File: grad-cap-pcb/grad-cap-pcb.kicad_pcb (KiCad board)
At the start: 2 copper layers, 323.3 x 323.3 mm, 146 parts

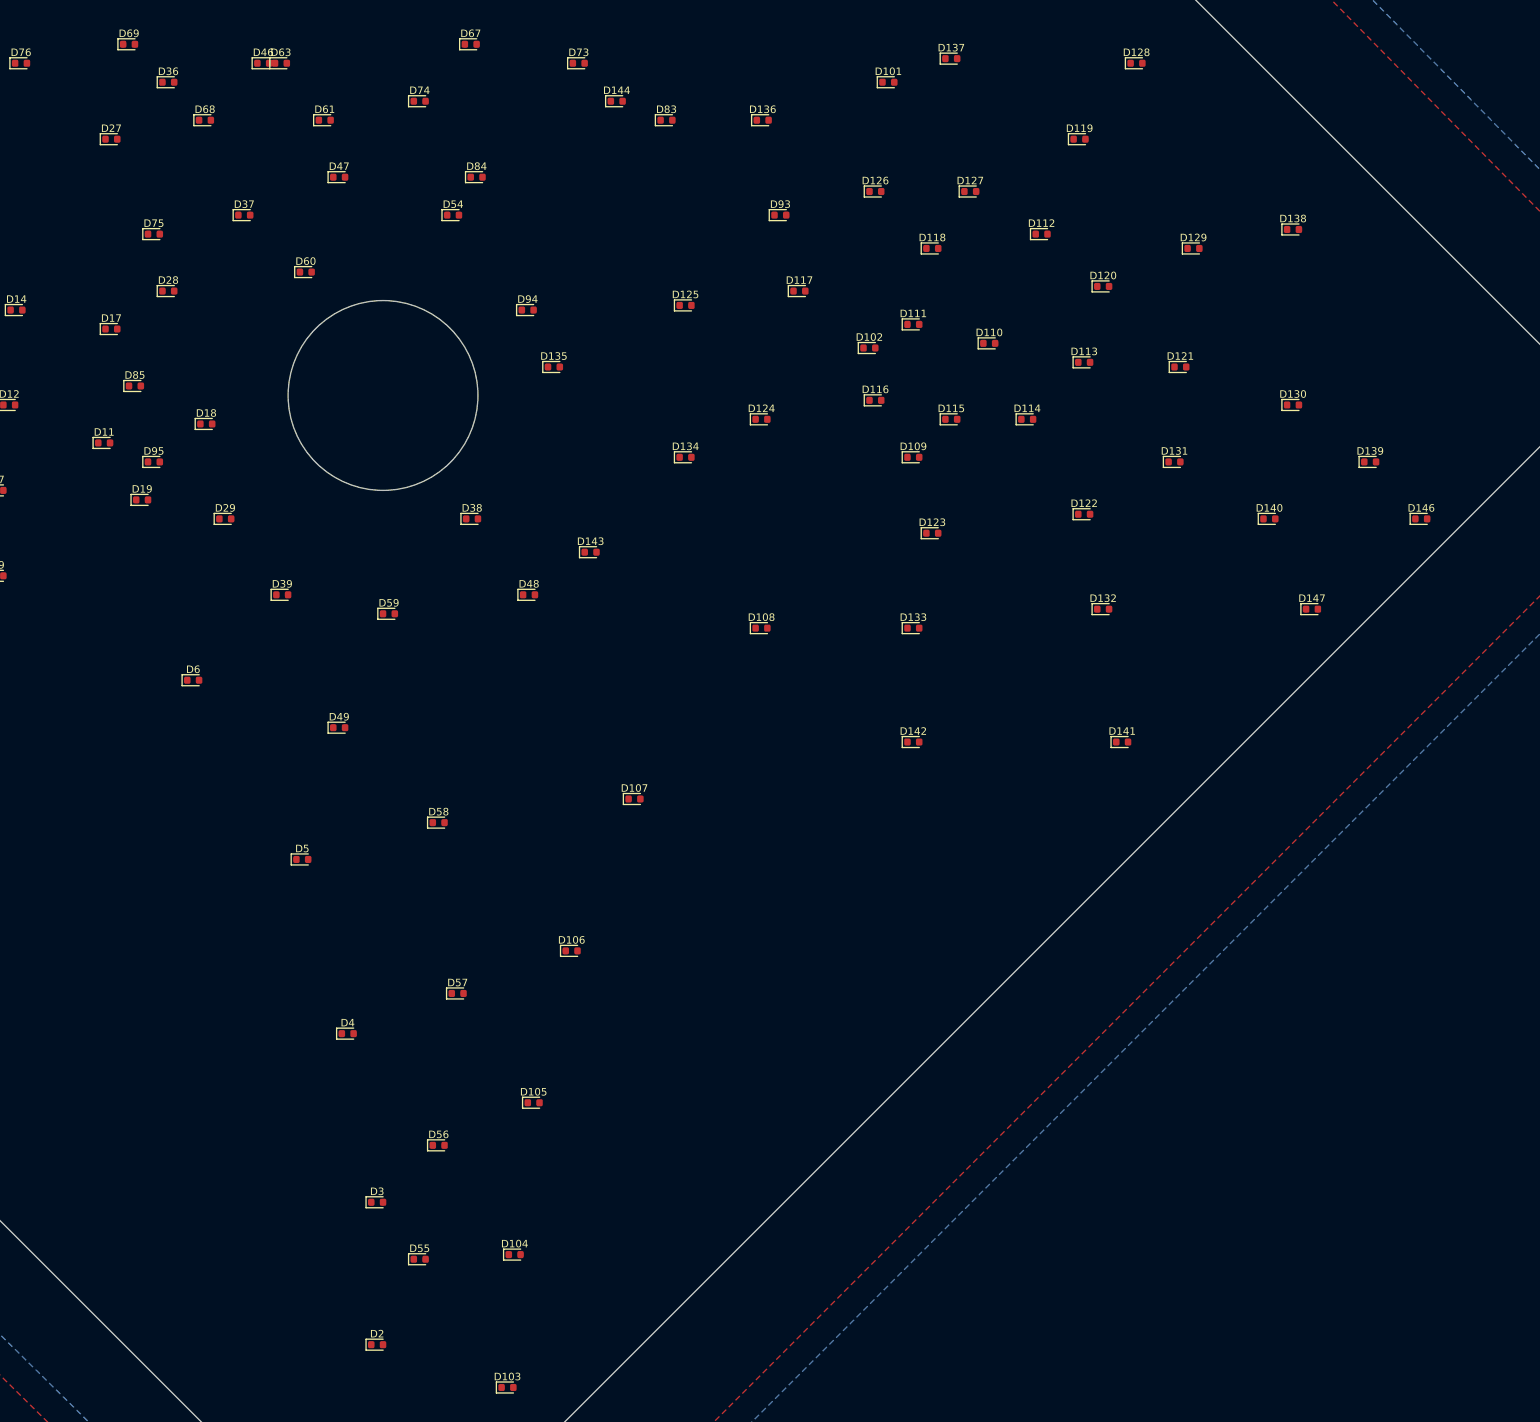
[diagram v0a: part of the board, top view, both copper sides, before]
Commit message: addd more
switched from npn to pnp to make the LEDs connect to the ground plane - easier routing.
added labels and or gates so the mosfets wouldnt trigger each other
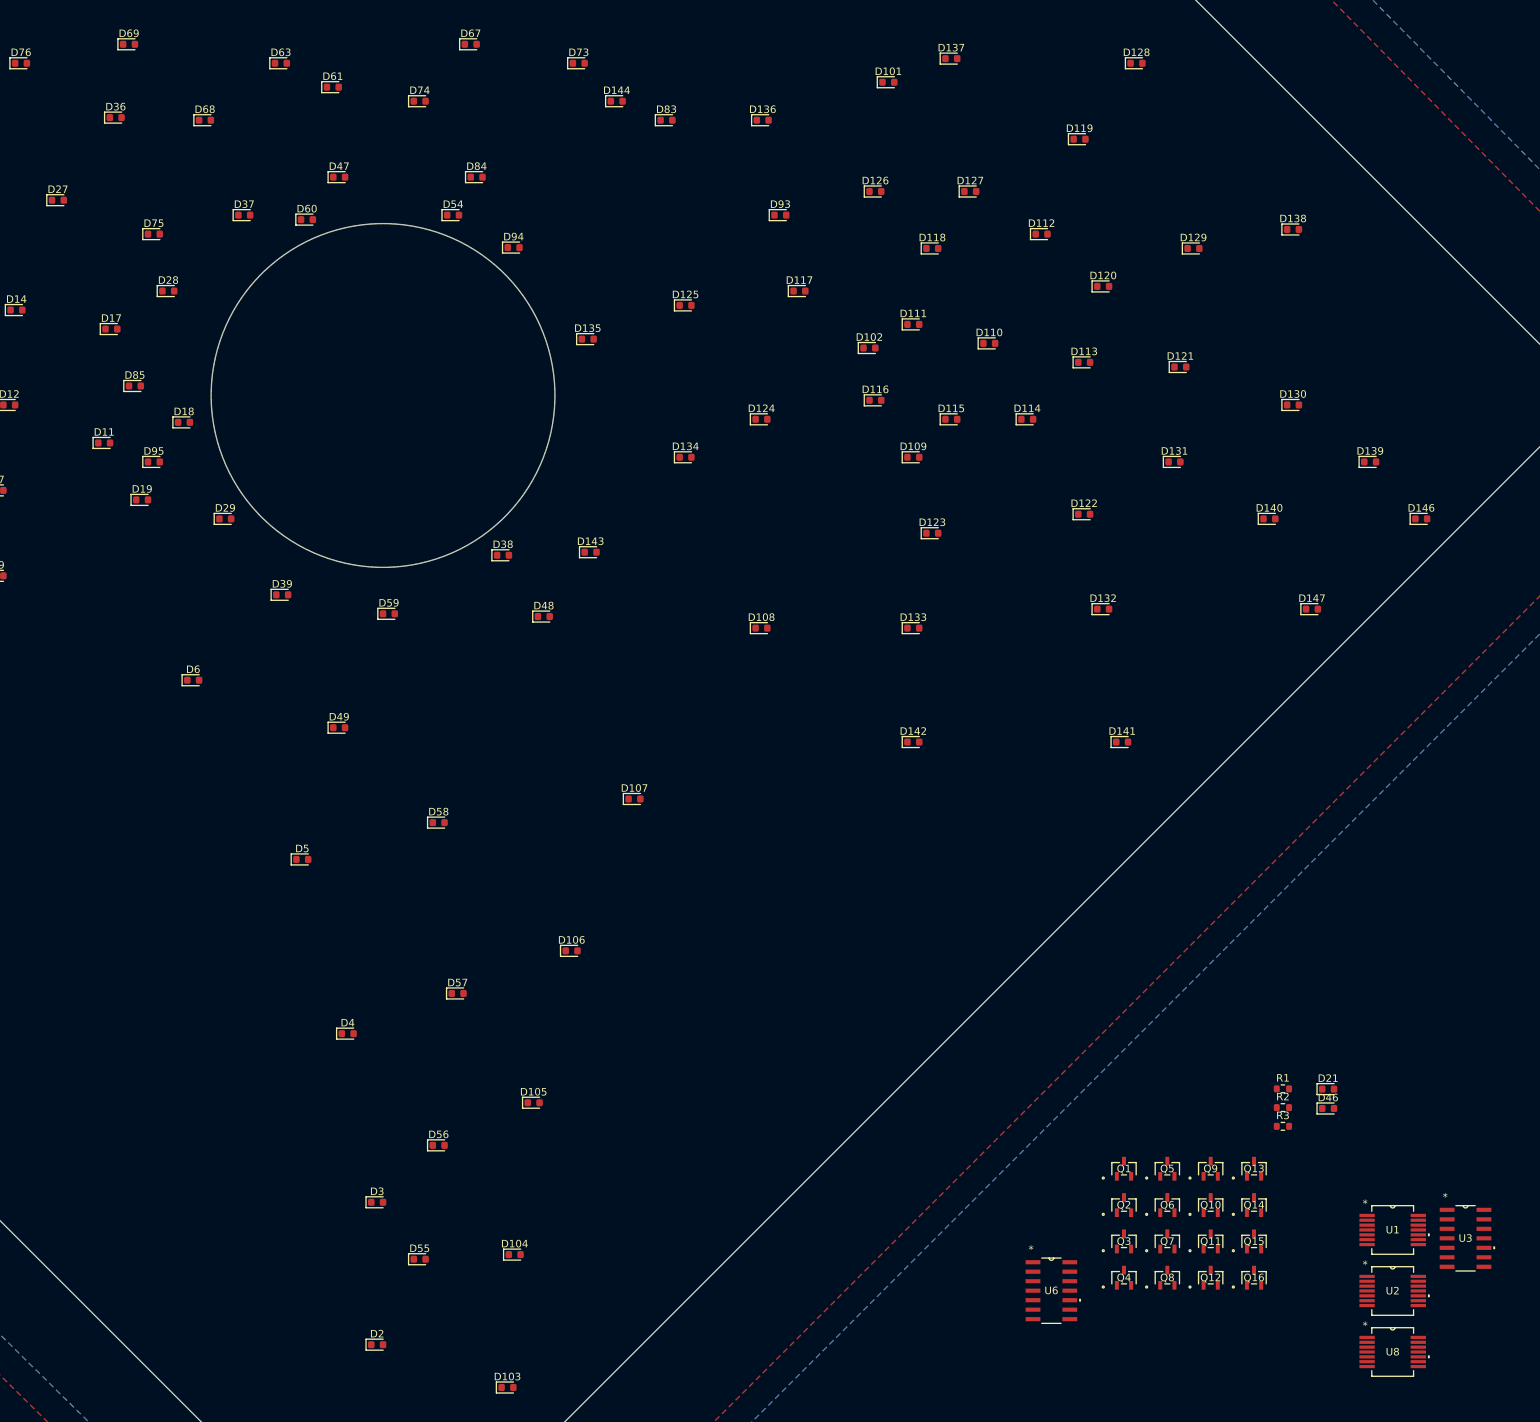
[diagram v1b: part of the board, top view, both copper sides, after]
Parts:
- added D21: LED, LED_SMD:LED_0603_1608Metric, F.Cu at (380.5, 315.1)
- added Q1: NPN, General Library:PN2907A, F.Cu at (353.1, 325.7)
- added Q10: NPN, General Library:PN2907A, F.Cu at (364.7, 330.6)
- added Q11: NPN, General Library:PN2907A, F.Cu at (364.7, 335.4)
- added Q12: NPN, General Library:PN2907A, F.Cu at (364.7, 340.3)
- added Q13: NPN, General Library:PN2907A, F.Cu at (370.5, 325.7)
- added Q14: NPN, General Library:PN2907A, F.Cu at (370.5, 330.6)
- added Q15: NPN, General Library:PN2907A, F.Cu at (370.5, 335.4)
- added Q16: NPN, General Library:PN2907A, F.Cu at (370.5, 340.3)
- added Q2: NPN, General Library:PN2907A, F.Cu at (353.1, 330.6)
- added Q3: NPN, General Library:PN2907A, F.Cu at (353.1, 335.4)
- added Q4: NPN, General Library:PN2907A, F.Cu at (353.1, 340.3)
- added Q5: NPN, General Library:PN2907A, F.Cu at (358.9, 325.7)
- added Q6: NPN, General Library:PN2907A, F.Cu at (358.9, 330.6)
- added Q7: NPN, General Library:PN2907A, F.Cu at (358.9, 335.4)
- added Q8: NPN, General Library:PN2907A, F.Cu at (358.9, 340.3)
- added Q9: NPN, General Library:PN2907A, F.Cu at (364.7, 325.7)
- added R1: 0 ohms, Resistor_SMD:R_0603_1608Metric, F.Cu at (374.4, 315.0)
- added R2: 0 ohms, Resistor_SMD:R_0603_1608Metric, F.Cu at (374.4, 317.5)
- added R3: 0 ohms, Resistor_SMD:R_0603_1608Metric, F.Cu at (374.4, 320.0)
- added U1: SN74AHCT32DBR, GRAD-CAP:SN74AHCT32DBR_2-INPUT-QUAD-OR, F.Cu at (389.1, 333.9)
- added U2: SN74AHCT32DBR, GRAD-CAP:SN74AHCT32DBR_2-INPUT-QUAD-OR, F.Cu at (389.1, 342.1)
- added U3: CD4072BM96, GRAD-CAP:CD4072BM96_4-INPUT-OR, F.Cu at (398.8, 335.0)
- added U6: CD4075BM96, GRAD-CAP:CD4075BM96-3IN-TRIO-OR, F.Cu at (343.4, 342.0)
- added U8: SN74AHCT32DBR, GRAD-CAP:SN74AHCT32DBR_2-INPUT-QUAD-OR, F.Cu at (389.1, 350.2)
- moved D46 199.6 mm to (380.5, 317.6)
- moved D27 10.9 mm to (210.5, 196.1)
- moved D94 8.57 mm to (271.5, 202.5)
- moved D36 8.49 mm to (218.2, 185.1)
- moved D60 7.02 mm to (243.8, 198.7)
- moved D38 6.39 mm to (270.1, 243.6)
- moved D135 5.87 mm to (281.4, 214.7)
- moved D61 4.55 mm to (247.3, 181.0)
- moved D48 3.52 mm to (275.5, 251.8)
- moved D18 2.99 mm to (227.4, 225.8)
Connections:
- D1 pad 1: unconnected-(D1-K-Pad1) -> /leds+mosfets/frame1
- D1 pad 2: unconnected-(D1-A-Pad2) -> +2V2
- D10 pad 1: unconnected-(D10-K-Pad1) -> /leds+mosfets/frame4
- D10 pad 2: unconnected-(D10-A-Pad2) -> +2V2
- D100 pad 1: unconnected-(D100-K-Pad1) -> /leds+mosfets/frame14
- D100 pad 2: unconnected-(D100-A-Pad2) -> +2V2
- D101 pad 1: unconnected-(D101-K-Pad1) -> /leds+mosfets/frame15
- D101 pad 2: unconnected-(D101-A-Pad2) -> +2V2
- D102 pad 1: unconnected-(D102-K-Pad1) -> /leds+mosfets/13or14
- D102 pad 2: unconnected-(D102-A-Pad2) -> +2V2
- D103 pad 1: unconnected-(D103-K-Pad1) -> /leds+mosfets/frame14
- D103 pad 2: unconnected-(D103-A-Pad2) -> +2V2
- D104 pad 1: unconnected-(D104-K-Pad1) -> /leds+mosfets/14or15
- D104 pad 2: unconnected-(D104-A-Pad2) -> +2V2
- D105 pad 1: unconnected-(D105-K-Pad1) -> /leds+mosfets/frame15
- D105 pad 2: unconnected-(D105-A-Pad2) -> +2V2
- D106 pad 1: unconnected-(D106-K-Pad1) -> /leds+mosfets/15or16
- D106 pad 2: unconnected-(D106-A-Pad2) -> +2V2
- D107 pad 1: unconnected-(D107-K-Pad1) -> /leds+mosfets/frame16
- D107 pad 2: unconnected-(D107-A-Pad2) -> +2V2
- D108 pad 1: unconnected-(D108-K-Pad1) -> /leds+mosfets/frame1
- D108 pad 2: unconnected-(D108-A-Pad2) -> +2V2
- D109 pad 1: unconnected-(D109-K-Pad1) -> /leds+mosfets/frame1
- D109 pad 2: unconnected-(D109-A-Pad2) -> +2V2
- D11 pad 1: unconnected-(D11-K-Pad1) -> /leds+mosfets/frame4
- D11 pad 2: unconnected-(D11-A-Pad2) -> +2V2
- D110 pad 1: unconnected-(D110-K-Pad1) -> /leds+mosfets/frame2
- D110 pad 2: unconnected-(D110-A-Pad2) -> +2V2
- D111 pad 1: unconnected-(D111-K-Pad1) -> /leds+mosfets/frame3
- D111 pad 2: unconnected-(D111-A-Pad2) -> +2V2
- D112 pad 1: unconnected-(D112-K-Pad1) -> /leds+mosfets/frame3
- D112 pad 2: unconnected-(D112-A-Pad2) -> +2V2
- D113 pad 1: unconnected-(D113-K-Pad1) -> /leds+mosfets/3or4
- D113 pad 2: unconnected-(D113-A-Pad2) -> +2V2
- D114 pad 1: unconnected-(D114-K-Pad1) -> /leds+mosfets/frame4
- D114 pad 2: unconnected-(D114-A-Pad2) -> +2V2
- D115 pad 1: unconnected-(D115-K-Pad1) -> /leds+mosfets/frame3
- D115 pad 2: unconnected-(D115-A-Pad2) -> +2V2
- D116 pad 1: unconnected-(D116-K-Pad1) -> /leds+mosfets/frame4
- D116 pad 2: unconnected-(D116-A-Pad2) -> +2V2
- D117 pad 1: unconnected-(D117-K-Pad1) -> /leds+mosfets/frame4
- D117 pad 2: unconnected-(D117-A-Pad2) -> +2V2
- D118 pad 1: unconnected-(D118-K-Pad1) -> /leds+mosfets/frame4
- D118 pad 2: unconnected-(D118-A-Pad2) -> +2V2
- D119 pad 1: unconnected-(D119-K-Pad1) -> /leds+mosfets/frame3
- D119 pad 2: unconnected-(D119-A-Pad2) -> +2V2
- D12 pad 1: unconnected-(D12-K-Pad1) -> /leds+mosfets/frame4
- D12 pad 2: unconnected-(D12-A-Pad2) -> +2V2
- D120 pad 1: unconnected-(D120-K-Pad1) -> /leds+mosfets/frame4
- D120 pad 2: unconnected-(D120-A-Pad2) -> +2V2
- D121 pad 1: unconnected-(D121-K-Pad1) -> /leds+mosfets/4or5
- D121 pad 2: unconnected-(D121-A-Pad2) -> +2V2
- D122 pad 1: unconnected-(D122-K-Pad1) -> /leds+mosfets/4or5
- D122 pad 2: unconnected-(D122-A-Pad2) -> +2V2
- D123 pad 1: unconnected-(D123-K-Pad1) -> /leds+mosfets/frame4
- D123 pad 2: unconnected-(D123-A-Pad2) -> +2V2
- D124 pad 1: unconnected-(D124-K-Pad1) -> /leds+mosfets/4or5
- D124 pad 2: unconnected-(D124-A-Pad2) -> +2V2
- D125 pad 1: unconnected-(D125-K-Pad1) -> /leds+mosfets/4or5
- D125 pad 2: unconnected-(D125-A-Pad2) -> +2V2
- D126 pad 1: unconnected-(D126-K-Pad1) -> /leds+mosfets/4or5
- D126 pad 2: unconnected-(D126-A-Pad2) -> +2V2
- D127 pad 1: unconnected-(D127-K-Pad1) -> /leds+mosfets/frame5
- D127 pad 2: unconnected-(D127-A-Pad2) -> +2V2
- D128 pad 1: unconnected-(D128-K-Pad1) -> /leds+mosfets/4or5
- D128 pad 2: unconnected-(D128-A-Pad2) -> +2V2
- D129 pad 1: unconnected-(D129-K-Pad1) -> /leds+mosfets/frame4
- D129 pad 2: unconnected-(D129-A-Pad2) -> +2V2
- D13 pad 1: unconnected-(D13-K-Pad1) -> /leds+mosfets/4or5
- D13 pad 2: unconnected-(D13-A-Pad2) -> +2V2
- D130 pad 1: unconnected-(D130-K-Pad1) -> /leds+mosfets/5or6
- D130 pad 2: unconnected-(D130-A-Pad2) -> +2V2
- D131 pad 1: unconnected-(D131-K-Pad1) -> /leds+mosfets/5or6
- D131 pad 2: unconnected-(D131-A-Pad2) -> +2V2
- D132 pad 1: unconnected-(D132-K-Pad1) -> /leds+mosfets/5or6
- D132 pad 2: unconnected-(D132-A-Pad2) -> +2V2
- D133 pad 1: unconnected-(D133-K-Pad1) -> /leds+mosfets/4or5
- D133 pad 2: unconnected-(D133-A-Pad2) -> +2V2
- D134 pad 1: unconnected-(D134-K-Pad1) -> /leds+mosfets/frame6
- D134 pad 2: unconnected-(D134-A-Pad2) -> +2V2
- D135 pad 1: unconnected-(D135-K-Pad1) -> /leds+mosfets/5or6
- D135 pad 2: unconnected-(D135-A-Pad2) -> +2V2
- D136 pad 1: unconnected-(D136-K-Pad1) -> /leds+mosfets/5or6
- D136 pad 2: unconnected-(D136-A-Pad2) -> +2V2
- D137 pad 1: unconnected-(D137-K-Pad1) -> /leds+mosfets/5or6
- D137 pad 2: unconnected-(D137-A-Pad2) -> +2V2
- D138 pad 1: unconnected-(D138-K-Pad1) -> /leds+mosfets/5or6
- D138 pad 2: unconnected-(D138-A-Pad2) -> +2V2
- D139 pad 1: unconnected-(D139-K-Pad1) -> /leds+mosfets/6or7
- D139 pad 2: unconnected-(D139-A-Pad2) -> +2V2
- D14 pad 1: unconnected-(D14-K-Pad1) -> /leds+mosfets/frame5
- D14 pad 2: unconnected-(D14-A-Pad2) -> +2V2
- D140 pad 1: unconnected-(D140-K-Pad1) -> /leds+mosfets/6or7
- D140 pad 2: unconnected-(D140-A-Pad2) -> +2V2
- D141 pad 1: unconnected-(D141-K-Pad1) -> /leds+mosfets/6or7
- D141 pad 2: unconnected-(D141-A-Pad2) -> +2V2
- D142 pad 1: unconnected-(D142-K-Pad1) -> /leds+mosfets/5or6or7or8
- D142 pad 2: unconnected-(D142-A-Pad2) -> +2V2
- D143 pad 1: unconnected-(D143-K-Pad1) -> /leds+mosfets/6or7or8
- D143 pad 2: unconnected-(D143-A-Pad2) -> +2V2
- D144 pad 1: unconnected-(D144-K-Pad1) -> /leds+mosfets/6or7or8
- D144 pad 2: unconnected-(D144-A-Pad2) -> +2V2
- D145 pad 1: unconnected-(D145-K-Pad1) -> /leds+mosfets/6or7
- D145 pad 2: unconnected-(D145-A-Pad2) -> +2V2
- D146 pad 1: unconnected-(D146-K-Pad1) -> /leds+mosfets/7or8
- D146 pad 2: unconnected-(D146-A-Pad2) -> +2V2
- D147 pad 1: unconnected-(D147-K-Pad1) -> /leds+mosfets/frame7
- D147 pad 2: unconnected-(D147-A-Pad2) -> +2V2
- D15 pad 1: unconnected-(D15-K-Pad1) -> /leds+mosfets/4or5
- D15 pad 2: unconnected-(D15-A-Pad2) -> +2V2
- D16 pad 1: unconnected-(D16-K-Pad1) -> /leds+mosfets/4or5
- D16 pad 2: unconnected-(D16-A-Pad2) -> +2V2
- D17 pad 1: unconnected-(D17-K-Pad1) -> /leds+mosfets/frame5
- D17 pad 2: unconnected-(D17-A-Pad2) -> +2V2
- D18 pad 1: unconnected-(D18-K-Pad1) -> /leds+mosfets/frame4
- D18 pad 2: unconnected-(D18-A-Pad2) -> +2V2
- D19 pad 2: unconnected-(D19-A-Pad2) -> GND
- D2 pad 1: unconnected-(D2-K-Pad1) -> /leds+mosfets/frame1
- D2 pad 2: unconnected-(D2-A-Pad2) -> +2V2
- D20 pad 1: unconnected-(D20-K-Pad1) -> /leds+mosfets/6or7
- D20 pad 2: unconnected-(D20-A-Pad2) -> +2V2
- D22 pad 1: unconnected-(D22-K-Pad1) -> /leds+mosfets/6or7
- D22 pad 2: unconnected-(D22-A-Pad2) -> +2V2
- D23 pad 1: unconnected-(D23-K-Pad1) -> /leds+mosfets/frame6
- D23 pad 2: unconnected-(D23-A-Pad2) -> +2V2
- D24 pad 1: unconnected-(D24-K-Pad1) -> /leds+mosfets/frame6
- D24 pad 2: unconnected-(D24-A-Pad2) -> +2V2
- D25 pad 1: unconnected-(D25-K-Pad1) -> /leds+mosfets/frame6
- D25 pad 2: unconnected-(D25-A-Pad2) -> +2V2
- D26 pad 1: unconnected-(D26-K-Pad1) -> /leds+mosfets/frame6
- D26 pad 2: unconnected-(D26-A-Pad2) -> +2V2
- D27 pad 1: unconnected-(D27-K-Pad1) -> /leds+mosfets/6or7
- D27 pad 2: unconnected-(D27-A-Pad2) -> +2V2
- D28 pad 1: unconnected-(D28-K-Pad1) -> /leds+mosfets/6or7
- D28 pad 2: unconnected-(D28-A-Pad2) -> +2V2
- D29 pad 1: unconnected-(D29-K-Pad1) -> /leds+mosfets/frame7
- D29 pad 2: unconnected-(D29-A-Pad2) -> +2V2
- D3 pad 1: unconnected-(D3-K-Pad1) -> /leds+mosfets/frame2
- D3 pad 2: unconnected-(D3-A-Pad2) -> +2V2
- D30 pad 1: unconnected-(D30-K-Pad1) -> /leds+mosfets/7or8
- D30 pad 2: unconnected-(D30-A-Pad2) -> +2V2
- D31 pad 1: unconnected-(D31-K-Pad1) -> /leds+mosfets/7or8
- D31 pad 2: unconnected-(D31-A-Pad2) -> +2V2
- D32 pad 1: unconnected-(D32-K-Pad1) -> /leds+mosfets/6or7
- D32 pad 2: unconnected-(D32-A-Pad2) -> +2V2
- D33 pad 1: unconnected-(D33-K-Pad1) -> /leds+mosfets/7or8
- D33 pad 2: unconnected-(D33-A-Pad2) -> +2V2
- D34 pad 1: unconnected-(D34-K-Pad1) -> /leds+mosfets/6or7
- D34 pad 2: unconnected-(D34-A-Pad2) -> +2V2
- D35 pad 1: unconnected-(D35-K-Pad1) -> /leds+mosfets/frame6
- D35 pad 2: unconnected-(D35-A-Pad2) -> +2V2
- D36 pad 1: unconnected-(D36-K-Pad1) -> /leds+mosfets/7or8
- D36 pad 2: unconnected-(D36-A-Pad2) -> +2V2
- D37 pad 1: unconnected-(D37-K-Pad1) -> /leds+mosfets/7or8
- D37 pad 2: unconnected-(D37-A-Pad2) -> +2V2
- D38 pad 1: unconnected-(D38-K-Pad1) -> /leds+mosfets/frame7
- D38 pad 2: unconnected-(D38-A-Pad2) -> +2V2
- D39 pad 1: unconnected-(D39-K-Pad1) -> /leds+mosfets/7or8
- D39 pad 2: unconnected-(D39-A-Pad2) -> +2V2
- D4 pad 1: unconnected-(D4-K-Pad1) -> /leds+mosfets/frame2
- D4 pad 2: unconnected-(D4-A-Pad2) -> +2V2
- D40 pad 1: unconnected-(D40-K-Pad1) -> /leds+mosfets/8or9
- D40 pad 2: unconnected-(D40-A-Pad2) -> +2V2
- D41 pad 1: unconnected-(D41-K-Pad1) -> /leds+mosfets/8or9
- D41 pad 2: unconnected-(D41-A-Pad2) -> +2V2
- D42 pad 1: unconnected-(D42-K-Pad1) -> /leds+mosfets/8or9
- D42 pad 2: unconnected-(D42-A-Pad2) -> +2V2
- D43 pad 1: unconnected-(D43-K-Pad1) -> /leds+mosfets/7or8or9
- D43 pad 2: unconnected-(D43-A-Pad2) -> +2V2
- D44 pad 1: unconnected-(D44-K-Pad1) -> /leds+mosfets/8or9
- D44 pad 2: unconnected-(D44-A-Pad2) -> +2V2
- D45 pad 1: unconnected-(D45-K-Pad1) -> /leds+mosfets/frame7
- D45 pad 2: unconnected-(D45-A-Pad2) -> +2V2
- D46 pad 2: unconnected-(D46-A-Pad2) -> GND
- D47 pad 1: unconnected-(D47-K-Pad1) -> /leds+mosfets/frame9
- D47 pad 2: unconnected-(D47-A-Pad2) -> +2V2
- D48 pad 1: unconnected-(D48-K-Pad1) -> /leds+mosfets/7or8
- D48 pad 2: unconnected-(D48-A-Pad2) -> +2V2
- D49 pad 1: unconnected-(D49-K-Pad1) -> /leds+mosfets/7or8
- D49 pad 2: unconnected-(D49-A-Pad2) -> +2V2
- D5 pad 1: unconnected-(D5-K-Pad1) -> /leds+mosfets/frame3
- D5 pad 2: unconnected-(D5-A-Pad2) -> +2V2
- D50 pad 1: unconnected-(D50-K-Pad1) -> /leds+mosfets/9or10
- D50 pad 2: unconnected-(D50-A-Pad2) -> +2V2
- D51 pad 1: unconnected-(D51-K-Pad1) -> /leds+mosfets/8or9or10
- D51 pad 2: unconnected-(D51-A-Pad2) -> +2V2
- D52 pad 1: unconnected-(D52-K-Pad1) -> /leds+mosfets/7or8or9
- D52 pad 2: unconnected-(D52-A-Pad2) -> +2V2
- D53 pad 1: unconnected-(D53-K-Pad1) -> /leds+mosfets/7or8
- D53 pad 2: unconnected-(D53-A-Pad2) -> +2V2
- D54 pad 1: unconnected-(D54-K-Pad1) -> /leds+mosfets/frame9
- D54 pad 2: unconnected-(D54-A-Pad2) -> +2V2
- D55 pad 1: unconnected-(D55-K-Pad1) -> /leds+mosfets/frame7
- D55 pad 2: unconnected-(D55-A-Pad2) -> +2V2
- D56 pad 1: unconnected-(D56-K-Pad1) -> /leds+mosfets/7or8
- D56 pad 2: unconnected-(D56-A-Pad2) -> +2V2
- D57 pad 1: unconnected-(D57-K-Pad1) -> /leds+mosfets/frame8
- D57 pad 2: unconnected-(D57-A-Pad2) -> +2V2
- D58 pad 1: unconnected-(D58-K-Pad1) -> /leds+mosfets/frame9
- D58 pad 2: unconnected-(D58-A-Pad2) -> +2V2
- D59 pad 1: unconnected-(D59-K-Pad1) -> /leds+mosfets/frame9
- D59 pad 2: unconnected-(D59-A-Pad2) -> +2V2
- D6 pad 1: unconnected-(D6-K-Pad1) -> /leds+mosfets/frame3
- D6 pad 2: unconnected-(D6-A-Pad2) -> +2V2
- D60 pad 1: unconnected-(D60-K-Pad1) -> /leds+mosfets/10or11
- D60 pad 2: unconnected-(D60-A-Pad2) -> +2V2
- D61 pad 1: unconnected-(D61-K-Pad1) -> /leds+mosfets/frame11
- D61 pad 2: unconnected-(D61-A-Pad2) -> +2V2
- D62 pad 1: unconnected-(D62-K-Pad1) -> /leds+mosfets/frame11
- D62 pad 2: unconnected-(D62-A-Pad2) -> +2V2
- D63 pad 1: unconnected-(D63-K-Pad1) -> /leds+mosfets/frame12
- D63 pad 2: unconnected-(D63-A-Pad2) -> +2V2
- D64 pad 1: unconnected-(D64-K-Pad1) -> /leds+mosfets/frame12
- D64 pad 2: unconnected-(D64-A-Pad2) -> +2V2
- D65 pad 1: unconnected-(D65-K-Pad1) -> /leds+mosfets/frame12
- D65 pad 2: unconnected-(D65-A-Pad2) -> +2V2
- D66 pad 1: unconnected-(D66-K-Pad1) -> /leds+mosfets/frame12
- D66 pad 2: unconnected-(D66-A-Pad2) -> +2V2
- D67 pad 1: unconnected-(D67-K-Pad1) -> /leds+mosfets/frame12
- D67 pad 2: unconnected-(D67-A-Pad2) -> +2V2
- D68 pad 1: unconnected-(D68-K-Pad1) -> /leds+mosfets/12or13
- D68 pad 2: unconnected-(D68-A-Pad2) -> +2V2
- D69 pad 1: unconnected-(D69-K-Pad1) -> /leds+mosfets/frame13
- D69 pad 2: unconnected-(D69-A-Pad2) -> +2V2
- D7 pad 1: unconnected-(D7-K-Pad1) -> /leds+mosfets/frame4
- D7 pad 2: unconnected-(D7-A-Pad2) -> +2V2
- D70 pad 1: unconnected-(D70-K-Pad1) -> /leds+mosfets/frame13
- D70 pad 2: unconnected-(D70-A-Pad2) -> +2V2
- D71 pad 1: unconnected-(D71-K-Pad1) -> /leds+mosfets/frame13
- D71 pad 2: unconnected-(D71-A-Pad2) -> +2V2
- D72 pad 1: unconnected-(D72-K-Pad1) -> /leds+mosfets/12or13
- D72 pad 2: unconnected-(D72-A-Pad2) -> +2V2
- D73 pad 1: unconnected-(D73-K-Pad1) -> /leds+mosfets/frame12
- D73 pad 2: unconnected-(D73-A-Pad2) -> +2V2
- D74 pad 1: unconnected-(D74-K-Pad1) -> /leds+mosfets/frame13
- D74 pad 2: unconnected-(D74-A-Pad2) -> +2V2
- D75 pad 1: unconnected-(D75-K-Pad1) -> /leds+mosfets/frame14
- D75 pad 2: unconnected-(D75-A-Pad2) -> +2V2
- D76 pad 1: unconnected-(D76-K-Pad1) -> /leds+mosfets/frame13
- D76 pad 2: unconnected-(D76-A-Pad2) -> +2V2
- D77 pad 1: unconnected-(D77-K-Pad1) -> /leds+mosfets/13or14
- D77 pad 2: unconnected-(D77-A-Pad2) -> +2V2
- D78 pad 1: unconnected-(D78-K-Pad1) -> /leds+mosfets/frame13
- D78 pad 2: unconnected-(D78-A-Pad2) -> +2V2
- D79 pad 1: unconnected-(D79-K-Pad1) -> /leds+mosfets/frame13
- D79 pad 2: unconnected-(D79-A-Pad2) -> +2V2
- D8 pad 1: unconnected-(D8-K-Pad1) -> /leds+mosfets/frame4
- D8 pad 2: unconnected-(D8-A-Pad2) -> +2V2
- D80 pad 1: unconnected-(D80-K-Pad1) -> /leds+mosfets/frame14
- D80 pad 2: unconnected-(D80-A-Pad2) -> +2V2
- D81 pad 1: unconnected-(D81-K-Pad1) -> /leds+mosfets/frame13
- D81 pad 2: unconnected-(D81-A-Pad2) -> +2V2
- D82 pad 1: unconnected-(D82-K-Pad1) -> /leds+mosfets/frame14
- D82 pad 2: unconnected-(D82-A-Pad2) -> +2V2
- D83 pad 1: unconnected-(D83-K-Pad1) -> /leds+mosfets/12or13
- D83 pad 2: unconnected-(D83-A-Pad2) -> +2V2
- D84 pad 1: unconnected-(D84-K-Pad1) -> /leds+mosfets/13or14
- D84 pad 2: unconnected-(D84-A-Pad2) -> +2V2
- D85 pad 1: unconnected-(D85-K-Pad1) -> /leds+mosfets/14or15
- D85 pad 2: unconnected-(D85-A-Pad2) -> +2V2
- D86 pad 1: unconnected-(D86-K-Pad1) -> /leds+mosfets/13or14
- D86 pad 2: unconnected-(D86-A-Pad2) -> +2V2
- D87 pad 1: unconnected-(D87-K-Pad1) -> /leds+mosfets/14or15
- D87 pad 2: unconnected-(D87-A-Pad2) -> +2V2
- D88 pad 1: unconnected-(D88-K-Pad1) -> /leds+mosfets/frame14
- D88 pad 2: unconnected-(D88-A-Pad2) -> +2V2
- D89 pad 1: unconnected-(D89-K-Pad1) -> /leds+mosfets/frame14
- D89 pad 2: unconnected-(D89-A-Pad2) -> +2V2
- D9 pad 1: unconnected-(D9-K-Pad1) -> /leds+mosfets/frame4
- D9 pad 2: unconnected-(D9-A-Pad2) -> +2V2
- D90 pad 1: unconnected-(D90-K-Pad1) -> /leds+mosfets/14or15
- D90 pad 2: unconnected-(D90-A-Pad2) -> +2V2
- D91 pad 1: unconnected-(D91-K-Pad1) -> /leds+mosfets/frame14
- D91 pad 2: unconnected-(D91-A-Pad2) -> +2V2
- D92 pad 1: unconnected-(D92-K-Pad1) -> /leds+mosfets/frame15
- D92 pad 2: unconnected-(D92-A-Pad2) -> +2V2
- D93 pad 1: unconnected-(D93-K-Pad1) -> /leds+mosfets/frame13
- D93 pad 2: unconnected-(D93-A-Pad2) -> +2V2
- D94 pad 1: unconnected-(D94-K-Pad1) -> /leds+mosfets/14or15
- D94 pad 2: unconnected-(D94-A-Pad2) -> +2V2
- D95 pad 1: unconnected-(D95-K-Pad1) -> /leds+mosfets/frame16
- D95 pad 2: unconnected-(D95-A-Pad2) -> +2V2
- D96 pad 1: unconnected-(D96-K-Pad1) -> /leds+mosfets/14or15
- D96 pad 2: unconnected-(D96-A-Pad2) -> +2V2
- D97 pad 1: unconnected-(D97-K-Pad1) -> /leds+mosfets/frame14
- D97 pad 2: unconnected-(D97-A-Pad2) -> +2V2
- D98 pad 1: unconnected-(D98-K-Pad1) -> /leds+mosfets/frame15
- D98 pad 2: unconnected-(D98-A-Pad2) -> +2V2
- D99 pad 1: unconnected-(D99-K-Pad1) -> /leds+mosfets/15or16
- D99 pad 2: unconnected-(D99-A-Pad2) -> +2V2
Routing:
- added copper zone on B.Cu, net GND
- added copper zone on F.Cu, net GND
- removed copper zone on B.Cu, net unconnected-(D39-A-Pad2)
- removed copper zone on F.Cu, net unconnected-(D39-A-Pad2)
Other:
- outline, holes or cut-outs redrawn
